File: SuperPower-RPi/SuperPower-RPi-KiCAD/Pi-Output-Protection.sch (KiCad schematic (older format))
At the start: 3 parts, among them Q4 2N7002-7-F, Q5 Q_PMOS_GSD

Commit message: Selected part for PMOS: DMP3056.
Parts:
- removed Q5: Q_PMOS_GSD, Package_TO_SOT_SMD:SOT-23, symbol Device:Q_PMOS_GSD
- added Q5: Q_PMOS_DMP3056L-7_SOT-23, Package_TO_SOT_SMD:SOT-23, symbol Manual_Lib:Q_PMOS_DMP3056L-7_SOT-23
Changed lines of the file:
@@
 	1    0    0    -1
-$EndComp
-$Comp
-L Device:Q_PMOS_GSD Q?
-U 1 1 5F703505
-P 5500 3350
-AR Path="/5F6AC644/5F703505" Ref="Q?"  Part="1"
-AR Path="/5F6AC517/5F703505" Ref="Q5"  Part="1"
-F 0 "Q5" V 5842 3350 50  0000 C CNN
-F 1 "Q_PMOS_GSD" V 5751 3350 50  0000 C CNN
-F 2 "Package_TO_SOT_SMD:SOT-23" H 5700 3450 50  0001 C CNN
-F 3 "~" H 5500 3350 50  0001 C CNN
-F 4 "FIX FOOTPRINT" H 5500 3350 50  0001 C CNN "Mfg"
-	1    5500 3350
-	0    1    -1   0
 $EndComp
 Text HLabel 4750 4050 0    50   Input ~ 0
@@
 Wire Wire Line
 	6100 3250 6350 3250
+$Comp
+L Manual_Lib:Q_PMOS_DMP3056L-7_SOT-23 Q5
+U 1 1 5FCD2BA8
+P 5500 3350
+F 0 "Q5" V 5842 3350 50  0000 C CNN
+F 1 "Q_PMOS_DMP3056L-7_SOT-23" H 5700 3300 50  0001 L CNN
+F 2 "Package_TO_SOT_SMD:SOT-23" H 5700 3450 50  0001 C CNN
+F 3 "https://www.diodes.com/assets/Datasheets/DMP3056L.pdf" H 5500 3350 50  0001 C CNN
+F 4 "Diodes Incorporated" H 5500 3350 50  0001 C CNN "Mfg"
+F 5 "DMP3056L-7" V 5751 3350 50  0000 C CNN "Mfg PN"
+F 6 "DMP3056L-7DICT-ND" H 5500 3350 50  0001 C CNN "Digi-Key PN"
+	1    5500 3350
+	0    1    -1   0
+$EndComp
 $EndSCHEMATC

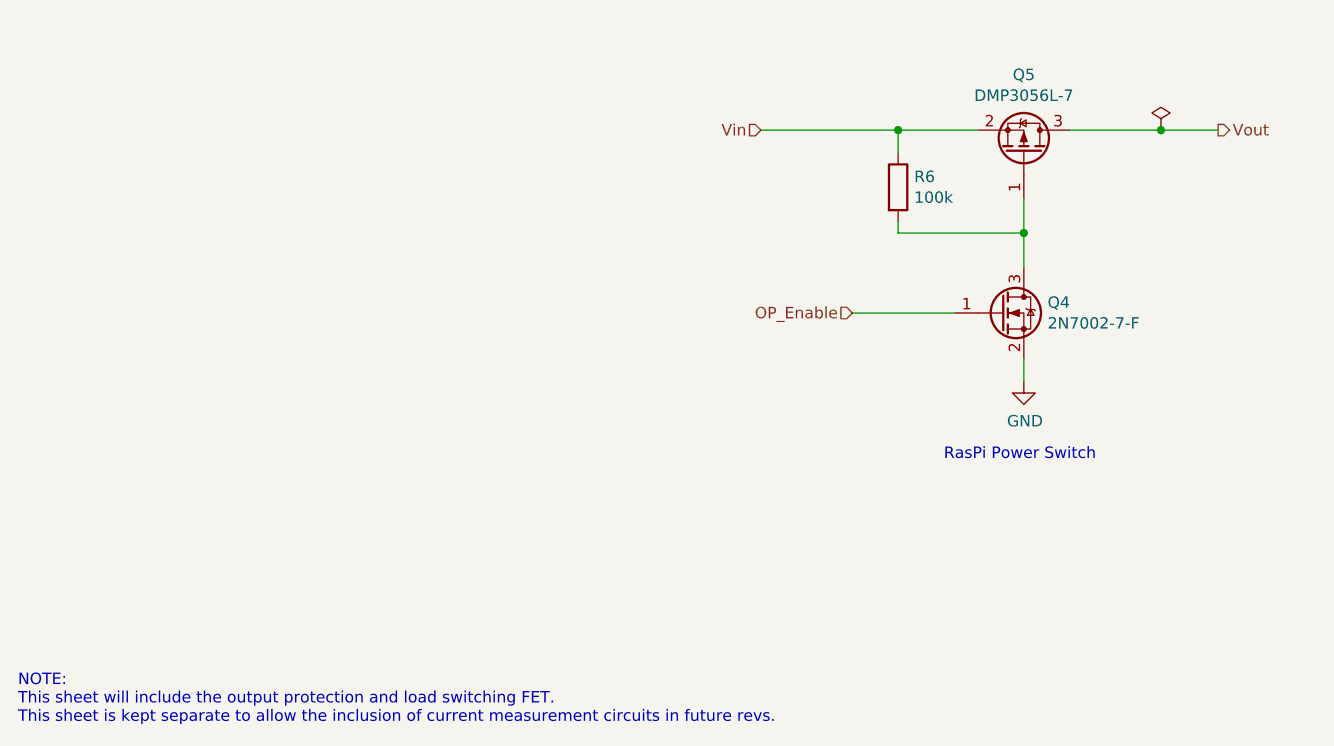
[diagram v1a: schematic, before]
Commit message: Added NCP380 to schematic, and removed redundant components.
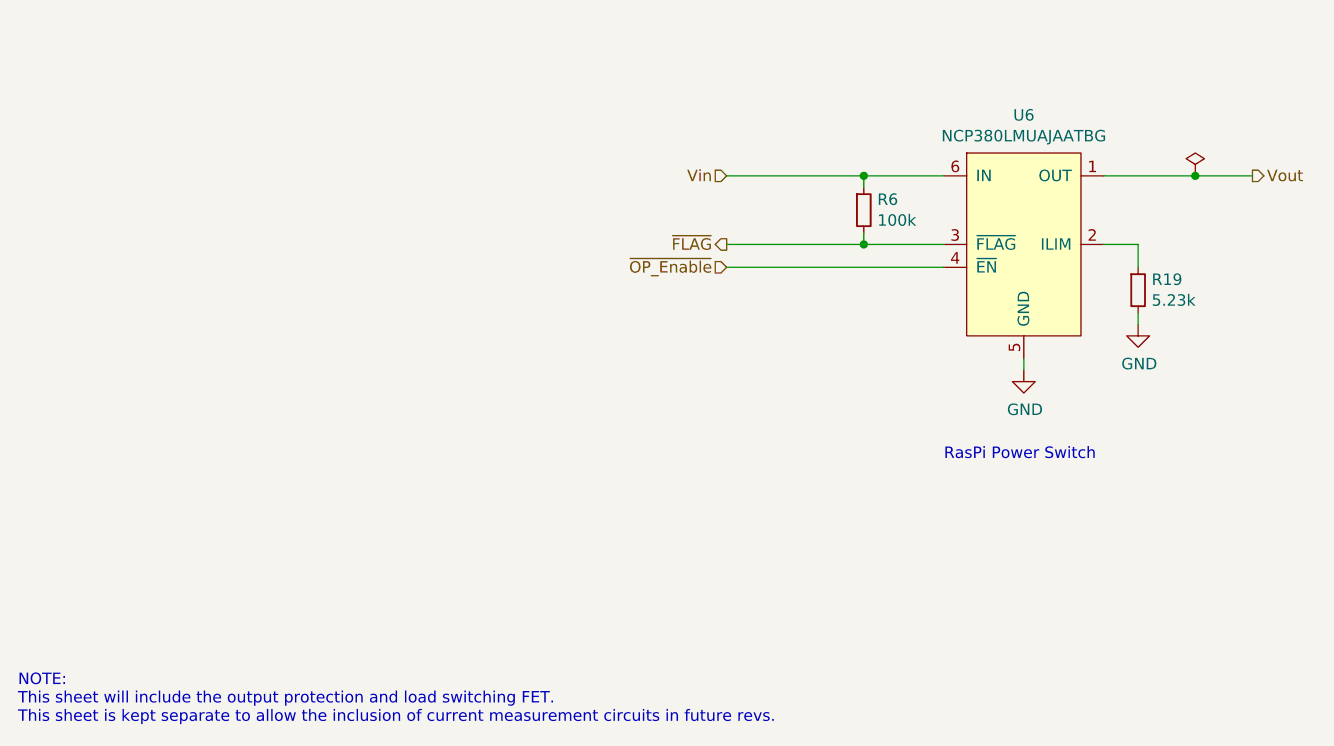
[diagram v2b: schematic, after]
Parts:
- removed Q4: 2N7002-7-F, Package_TO_SOT_SMD:SOT-23, symbol Device:Q_NMOS_GSD
- removed Q5: Q_PMOS_DMP3056L-7_SOT-23, Package_TO_SOT_SMD:SOT-23, symbol Manual_Lib:Q_PMOS_DMP3056L-7_SOT-23
- removed R6: 100k, Resistor_SMD:R_0402_1005Metric, symbol Device:R
- added R19: 5.23k, Resistor_SMD:R_0603_1608Metric, symbol Device:R_Small
- added R6: 100k, Resistor_SMD:R_0402_1005Metric, symbol Device:R_Small
- added U6: NCP380LMUAJAATBG, Package_DFN_QFN:DFN-6-1EP_3x3mm_P0.95mm_EP1.7x2.6mm, symbol Manual_Lib:NCP380LMUAJAATBG
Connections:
- net GND: now also R19.2, U6.5 (GND), U6.7 (PAD)
- net Vin: now also R6.1, U6.6 (IN)
- net Vout: now also U6.1 (OUT)
- new net: R19.1, U6.2 (ILIM)
- new net ~FLAG: R6.2, U6.3 (~FLAG)
- new net ~OP_Enable: U6.4 (~EN)
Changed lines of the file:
@@
 RasPi Power Switch
 Wire Wire Line
-	5700 3250 6100 3250
-Wire Wire Line
-	5500 4350 5500 4250
+	5500 4300 5500 4250
 $Comp
 L power:GND #PWR08
 U 1 1 5F704A6C
-P 5500 4350
-F 0 "#PWR08" H 5500 4100 50  0001 C CNN
-F 1 "GND" H 5505 4177 50  0000 C CNN
-F 2 "" H 5500 4350 50  0001 C CNN
-F 3 "" H 5500 4350 50  0001 C CNN
-	1    5500 4350
+P 5500 4300
+F 0 "#PWR08" H 5500 4050 50  0001 C CNN
+F 1 "GND" H 5505 4127 50  0000 C CNN
+F 2 "" H 5500 4300 50  0001 C CNN
+F 3 "" H 5500 4300 50  0001 C CNN
+	1    5500 4300
+	1    0    0    -1
+$EndComp
+Text HLabel 4200 3850 0    50   Input ~ 0
+~OP_Enable
+Wire Wire Line
+	5850 3450 6250 3450
+$Comp
+L power:PWR_FLAG #FLG0103
+U 1 1 5F7A8B93
+P 6250 3450
+F 0 "#FLG0103" H 6250 3525 50  0001 C CNN
+F 1 "PWR_FLAG" H 6250 3623 50  0001 C CNN
+F 2 "" H 6250 3450 50  0001 C CNN
+F 3 "~" H 6250 3450 50  0001 C CNN
+	1    6250 3450
+	1    0    0    -1
+$EndComp
+Connection ~ 6250 3450
+Wire Wire Line
+	6250 3450 6500 3450
+Text HLabel 6500 3450 2    50   Output ~ 0
+Vout
+Text HLabel 4200 3450 0    50   Input ~ 0
+Vin
+Wire Wire Line
+	4200 3450 4800 3450
+$Comp
+L Device:R_Small R6
+U 1 1 5FD73926
+P 4800 3600
+F 0 "R6" H 4859 3646 50  0000 L CNN
+F 1 "100k" H 4859 3555 50  0000 L CNN
+F 2 "Resistor_SMD:R_0402_1005Metric" H 4800 3600 50  0001 C CNN
+F 3 "~" H 4800 3600 50  0001 C CNN
+	1    4800 3600
 	1    0    0    -1
 $EndComp
 Wire Wire Line
-	5200 4050 4750 4050
-Connection ~ 5500 3700
+	5150 3750 4800 3750
 Wire Wire Line
-	5500 3700 5500 3550
+	4800 3750 4800 3700
 Wire Wire Line
-	5500 3700 5500 3850
+	4800 3500 4800 3450
+Connection ~ 4800 3450
 Wire Wire Line
-	4950 3700 5500 3700
-Wire Wire Line
-	4950 3650 4950 3700
+	4800 3450 5150 3450
 $Comp
-L Device:Q_NMOS_GSD Q4
-U 1 1 5F703D5E
-P 5400 4050
-F 0 "Q4" H 5604 4096 50  0000 L CNN
-F 1 "2N7002-7-F" H 5604 4005 50  0000 L CNN
-F 2 "Package_TO_SOT_SMD:SOT-23" H 5600 4150 50  0001 C CNN
-F 3 "~" H 5400 4050 50  0001 C CNN
-F 4 "Diodes Incorporated" H 5400 4050 50  0001 C CNN "Mfg"
-F 5 "2N7002-FDICT-ND" H 5400 4050 50  0001 C CNN "Digi-Key PN"
-F 6 "2N7002-7-F" H 5400 4050 50  0001 C CNN "Mfg PN"
-	1    5400 4050
+L Device:R_Small R19
+U 1 1 5FD75F9B
+P 6000 3950
+F 0 "R19" H 6059 3996 50  0000 L CNN
+F 1 "5.23k" H 6059 3905 50  0000 L CNN
+F 2 "Resistor_SMD:R_0603_1608Metric" H 6000 3950 50  0001 C CNN
+F 3 "~" H 6000 3950 50  0001 C CNN
+	1    6000 3950
 	1    0    0    -1
 $EndComp
-Connection ~ 4950 3250
 Wire Wire Line
-	4950 3250 4350 3250
+	6000 3850 6000 3750
 Wire Wire Line
-	4950 3250 5300 3250
-Wire Wire Line
-	4950 3350 4950 3250
+	6000 3750 5850 3750
 $Comp
-L Device:R R6
-U 1 1 5F70368F
-P 4950 3500
-F 0 "R6" H 5020 3546 50  0000 L CNN
-F 1 "100k" H 5020 3455 50  0000 L CNN
-F 2 "Resistor_SMD:R_0402_1005Metric" V 4880 3500 50  0001 C CNN
-F 3 "~" H 4950 3500 50  0001 C CNN
-F 4 "" H 4950 3500 50  0001 C CNN "Digi-Key PN"
-F 5 "" H 4950 3500 50  0001 C CNN "Mfg"
-F 6 "" H 4950 3500 50  0001 C CNN "Mfg PN"
-	1    4950 3500
+L power:GND #PWR050
+U 1 1 5FD76C02
+P 6000 4100
+F 0 "#PWR050" H 6000 3850 50  0001 C CNN
+F 1 "GND" H 6005 3927 50  0000 C CNN
+F 2 "" H 6000 4100 50  0001 C CNN
+F 3 "" H 6000 4100 50  0001 C CNN
+	1    6000 4100
 	1    0    0    -1
 $EndComp
-Text HLabel 4750 4050 0    50   Input ~ 0
-OP_Enable
-Text HLabel 6350 3250 2    50   Output ~ 0
-Vout
-Text HLabel 4350 3250 0    50   Input ~ 0
-Vin
+Wire Wire Line
+	6000 4100 6000 4050
+Wire Wire Line
+	4200 3850 5150 3850
+Wire Wire Line
+	4800 3750 4200 3750
+Connection ~ 4800 3750
+Text HLabel 4200 3750 0    50   Output ~ 0
+~FLAG
 $Comp
-L power:PWR_FLAG #FLG0103
-U 1 1 5F7A8B93
-P 6100 3250
-F 0 "#FLG0103" H 6100 3325 50  0001 C CNN
-F 1 "PWR_FLAG" H 6100 3423 50  0001 C CNN
-F 2 "" H 6100 3250 50  0001 C CNN
-F 3 "~" H 6100 3250 50  0001 C CNN
-	1    6100 3250
+L Manual_Lib:NCP380LMUAJAATBG U6
+U 1 1 5FD6E3A9
+P 5500 3650
+F 0 "U6" H 5500 4115 50  0000 C CNN
+F 1 "NCP380LMUAJAATBG" H 5500 4024 50  0000 C CNN
+F 2 "Package_DFN_QFN:DFN-6-1EP_3x3mm_P0.95mm_EP1.7x2.6mm" H 5550 3800 50  0001 C CNN
+F 3 "https://www.onsemi.com/pub/Collateral/NCP380-D.PDF" H 5550 3800 50  0001 C CNN
+F 4 "On Semi" H 5500 3650 50  0001 C CNN "Mfg"
+F 5 "NCP380LMUAJAATBG" H 5500 3650 50  0001 C CNN "Mfg PN"
+F 6 "NCP380LMUAJAATBGOSCT-ND" H 5500 3650 50  0001 C CNN "Digi-Key PN"
+	1    5500 3650
 	1    0    0    -1
 $EndComp
-Connection ~ 6100 3250
-Wire Wire Line
-	6100 3250 6350 3250
-$Comp
-L Manual_Lib:Q_PMOS_DMP3056L-7_SOT-23 Q5
-U 1 1 5FCD2BA8
-P 5500 3350
-F 0 "Q5" V 5842 3350 50  0000 C CNN
-F 1 "Q_PMOS_DMP3056L-7_SOT-23" H 5700 3300 50  0001 L CNN
-F 2 "Package_TO_SOT_SMD:SOT-23" H 5700 3450 50  0001 C CNN
-F 3 "https://www.diodes.com/assets/Datasheets/DMP3056L.pdf" H 5500 3350 50  0001 C CNN
-F 4 "Diodes Incorporated" H 5500 3350 50  0001 C CNN "Mfg"
-F 5 "DMP3056L-7" V 5751 3350 50  0000 C CNN "Mfg PN"
-F 6 "DMP3056L-7DICT-ND" H 5500 3350 50  0001 C CNN "Digi-Key PN"
-	1    5500 3350
-	0    1    -1   0
-$EndComp
 $EndSCHEMATC

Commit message: Updated Footprint ref of NCP380 to use custom footprint.
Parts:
- U6: footprint Package_DFN_QFN:DFN-6-1EP_3x3mm_P0.95mm_EP1.7x2.6mm -> SuperPower-RPi-KiCAD:UDFN-6-1EP_2x2mm_P0.65mm_EP0.95x1.7mm
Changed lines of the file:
@@
 F 0 "U6" H 5500 4115 50  0000 C CNN
 F 1 "NCP380LMUAJAATBG" H 5500 4024 50  0000 C CNN
-F 2 "Package_DFN_QFN:DFN-6-1EP_3x3mm_P0.95mm_EP1.7x2.6mm" H 5550 3800 50  0001 C CNN
+F 2 "SuperPower-RPi-KiCAD:UDFN-6-1EP_2x2mm_P0.65mm_EP0.95x1.7mm" H 5550 3800 50  0001 C CNN
 F 3 "https://www.onsemi.com/pub/Collateral/NCP380-D.PDF" H 5550 3800 50  0001 C CNN
 F 4 "On Semi" H 5500 3650 50  0001 C CNN "Mfg"

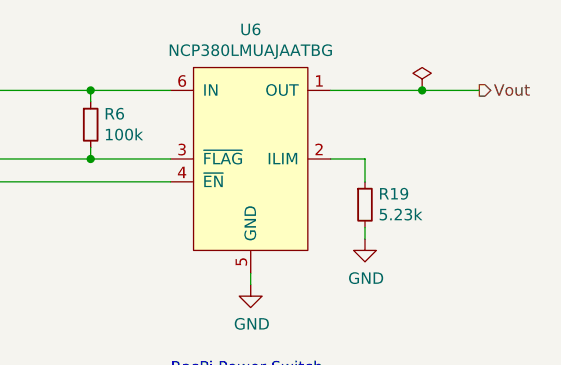
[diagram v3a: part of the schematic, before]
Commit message: Removed power flag to prevent ERC error.
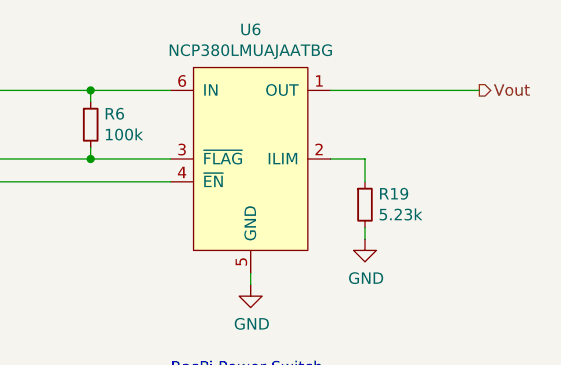
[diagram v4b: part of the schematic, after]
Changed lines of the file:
@@
 Text HLabel 4200 3850 0    50   Input ~ 0
 ~OP_Enable
-Wire Wire Line
-	5850 3450 6250 3450
-$Comp
-L power:PWR_FLAG #FLG0103
-U 1 1 5F7A8B93
-P 6250 3450
-F 0 "#FLG0103" H 6250 3525 50  0001 C CNN
-F 1 "PWR_FLAG" H 6250 3623 50  0001 C CNN
-F 2 "" H 6250 3450 50  0001 C CNN
-F 3 "~" H 6250 3450 50  0001 C CNN
-	1    6250 3450
-	1    0    0    -1
-$EndComp
-Connection ~ 6250 3450
-Wire Wire Line
-	6250 3450 6500 3450
 Text HLabel 6500 3450 2    50   Output ~ 0
 Vout
@@
 	1    0    0    -1
 $EndComp
+Wire Wire Line
+	5850 3450 6500 3450
 $EndSCHEMATC

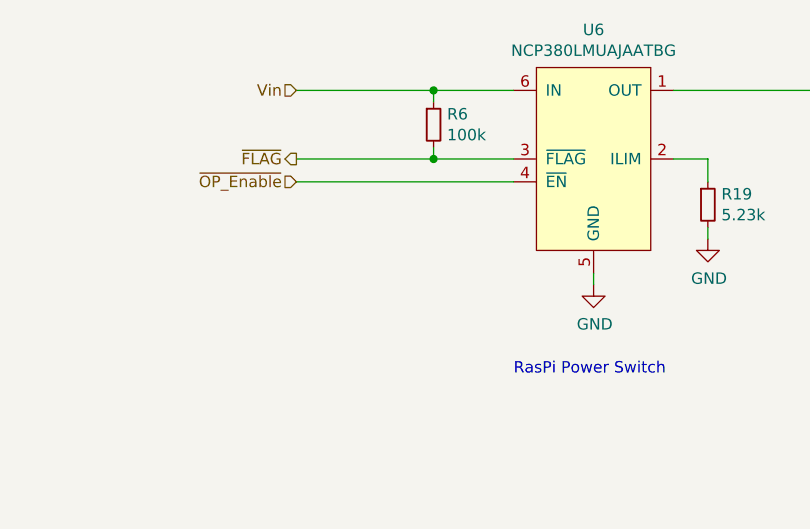
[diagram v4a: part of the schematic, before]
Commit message: Added Pull Down to RasPi Power Switch ~Enable line.
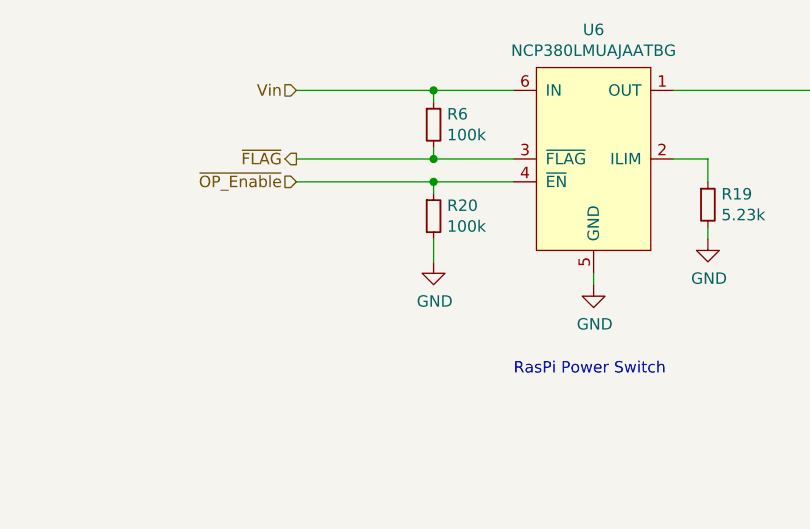
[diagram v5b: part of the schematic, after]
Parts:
- added R20: 100k, Resistor_SMD:R_0402_1005Metric, symbol Device:R_Small
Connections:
- net GND: now also R20.2
- net ~OP_Enable: now also R20.1
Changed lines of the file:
@@
 	6000 4100 6000 4050
 Wire Wire Line
-	4200 3850 5150 3850
+	4200 3850 4800 3850
 Wire Wire Line
 	4800 3750 4200 3750
@@
 Wire Wire Line
 	5850 3450 6500 3450
+$Comp
+L Device:R_Small R20
+U 1 1 5FE4EBC2
+P 4800 4000
+F 0 "R20" H 4859 4046 50  0000 L CNN
+F 1 "100k" H 4859 3955 50  0000 L CNN
+F 2 "Resistor_SMD:R_0402_1005Metric" H 4800 4000 50  0001 C CNN
+F 3 "~" H 4800 4000 50  0001 C CNN
+	1    4800 4000
+	1    0    0    -1
+$EndComp
+Wire Wire Line
+	4800 3900 4800 3850
+Connection ~ 4800 3850
+Wire Wire Line
+	4800 3850 5150 3850
+$Comp
+L power:GND #PWR051
+U 1 1 5FE4EF9E
+P 4800 4200
+F 0 "#PWR051" H 4800 3950 50  0001 C CNN
+F 1 "GND" H 4805 4027 50  0000 C CNN
+F 2 "" H 4800 4200 50  0001 C CNN
+F 3 "" H 4800 4200 50  0001 C CNN
+	1    4800 4200
+	1    0    0    -1
+$EndComp
+Wire Wire Line
+	4800 4200 4800 4100
 $EndSCHEMATC

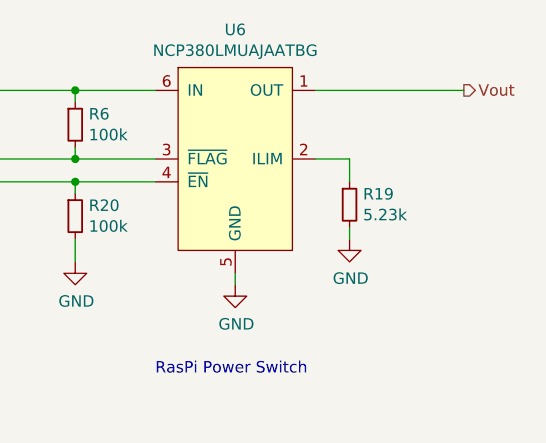
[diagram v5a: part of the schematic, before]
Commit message: Added 2 TP, voltage divider for input power, and moved battery connector flush to edge of board.
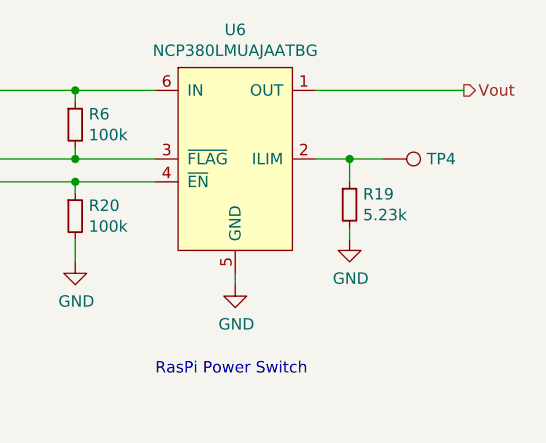
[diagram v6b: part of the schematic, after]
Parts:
- added TP4: DNP, TestPoint:TestPoint_Pad_1.0x1.0mm, symbol Connector:TestPoint
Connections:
- net at R19.1, U6.2 (ILIM): now also TP4.1
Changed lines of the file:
@@
 Wire Wire Line
 	4800 4200 4800 4100
+$Comp
+L Connector:TestPoint TP?
+U 1 1 5FF08CAB
+P 6150 3750
+AR Path="/5F6AC481/5FF08CAB" Ref="TP?"  Part="1"
+AR Path="/5F6AC4E0/5FF08CAB" Ref="TP?"  Part="1"
+AR Path="/5F6AC517/5FF08CAB" Ref="TP4"  Part="1"
+F 0 "TP4" V 6150 3938 50  0000 L CNN
+F 1 "DNP" H 6208 3777 50  0001 L CNN
+F 2 "TestPoint:TestPoint_Pad_1.0x1.0mm" H 6350 3750 50  0001 C CNN
+F 3 "~" H 6350 3750 50  0001 C CNN
+F 4 "DNP" H 6150 3750 50  0001 C CNN "Mfg"
+	1    6150 3750
+	0    1    1    0
+$EndComp
+Wire Wire Line
+	6150 3750 6000 3750
+Connection ~ 6000 3750
 $EndSCHEMATC

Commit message: Updated schematic to fill out all BOM entries.
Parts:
- R19: Digi-Key PN (none) -> 311-5.23KHRCT-ND; Mfg (none) -> Yageo; Mfg PN (none) -> RC0603FR-075K23L
- R20, R6: Digi-Key PN (none) -> 311-100KLRCT-ND; Mfg (none) -> Yageo; Mfg PN (none) -> RC0402FR-07100KL
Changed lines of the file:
@@
 F 2 "Resistor_SMD:R_0402_1005Metric" H 4800 3600 50  0001 C CNN
 F 3 "~" H 4800 3600 50  0001 C CNN
+F 4 "311-100KLRCT-ND" H 4800 3600 50  0001 C CNN "Digi-Key PN"
+F 5 "Yageo" H 4800 3600 50  0001 C CNN "Mfg"
+F 6 "RC0402FR-07100KL" H 4800 3600 50  0001 C CNN "Mfg PN"
 	1    4800 3600
 	1    0    0    -1
@@
 F 2 "Resistor_SMD:R_0603_1608Metric" H 6000 3950 50  0001 C CNN
 F 3 "~" H 6000 3950 50  0001 C CNN
+F 4 "311-5.23KHRCT-ND" H 6000 3950 50  0001 C CNN "Digi-Key PN"
+F 5 "Yageo" H 6000 3950 50  0001 C CNN "Mfg"
+F 6 "RC0603FR-075K23L" H 6000 3950 50  0001 C CNN "Mfg PN"
 	1    6000 3950
 	1    0    0    -1
@@
 F 2 "Resistor_SMD:R_0402_1005Metric" H 4800 4000 50  0001 C CNN
 F 3 "~" H 4800 4000 50  0001 C CNN
+F 4 "311-100KLRCT-ND" H 4800 4000 50  0001 C CNN "Digi-Key PN"
+F 5 "Yageo" H 4800 4000 50  0001 C CNN "Mfg"
+F 6 "RC0402FR-07100KL" H 4800 4000 50  0001 C CNN "Mfg PN"
 	1    4800 4000
 	1    0    0    -1
